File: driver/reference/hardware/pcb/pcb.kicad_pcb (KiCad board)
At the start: 2 copper layers, 122 x 122 mm, 50 parts, among them J1 USB_B_Micro, J2 USB_A, J3 USB_A, J4 USB_A, M1 Fan, Q1 S8050, SW1 SW_Push, U1 locked, U2 AT89C52, U3 SL2.1A, U4 LCD1602, Y1 11.0592MHz, Y2 12MHz

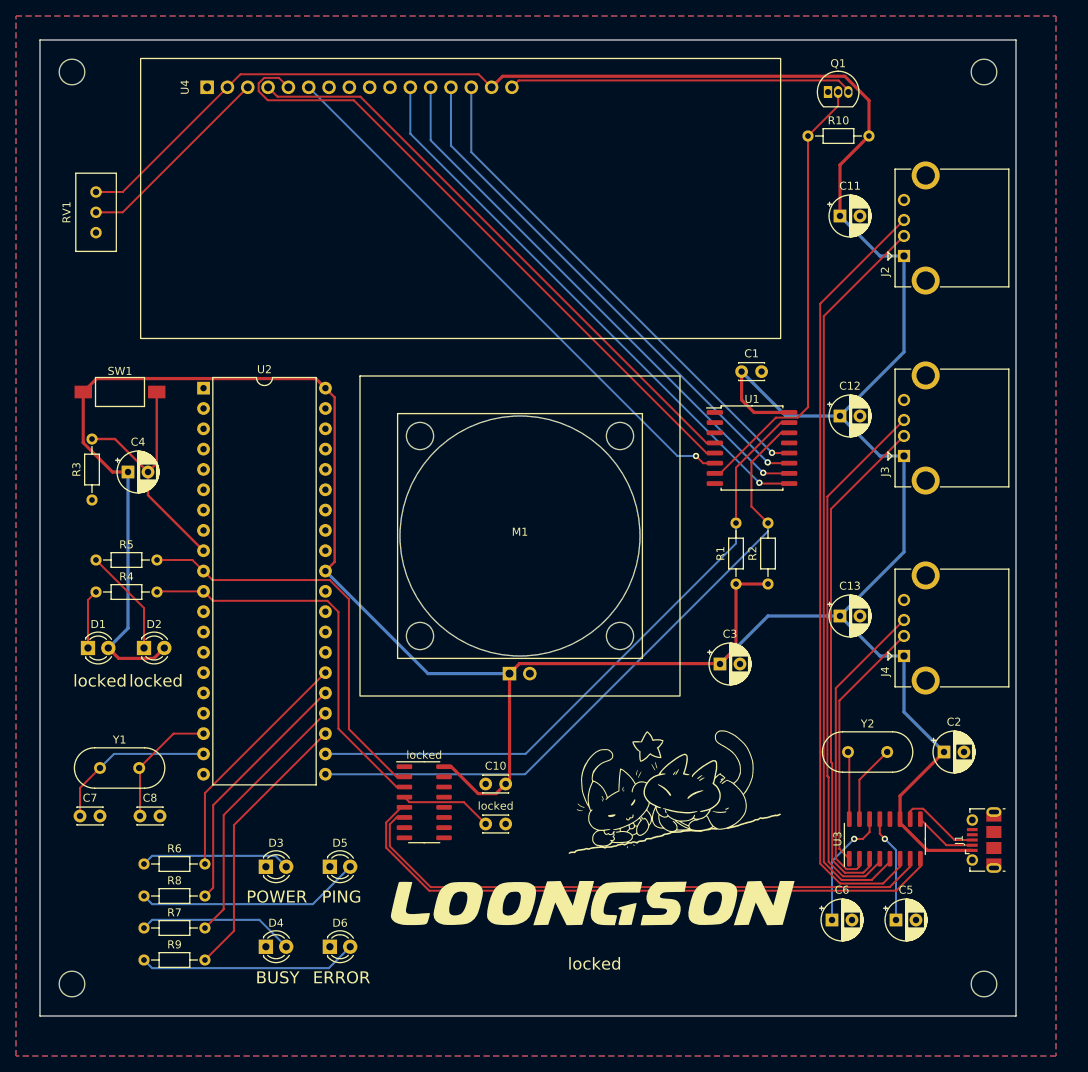
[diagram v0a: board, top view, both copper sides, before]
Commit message: Basic implementation of frontend
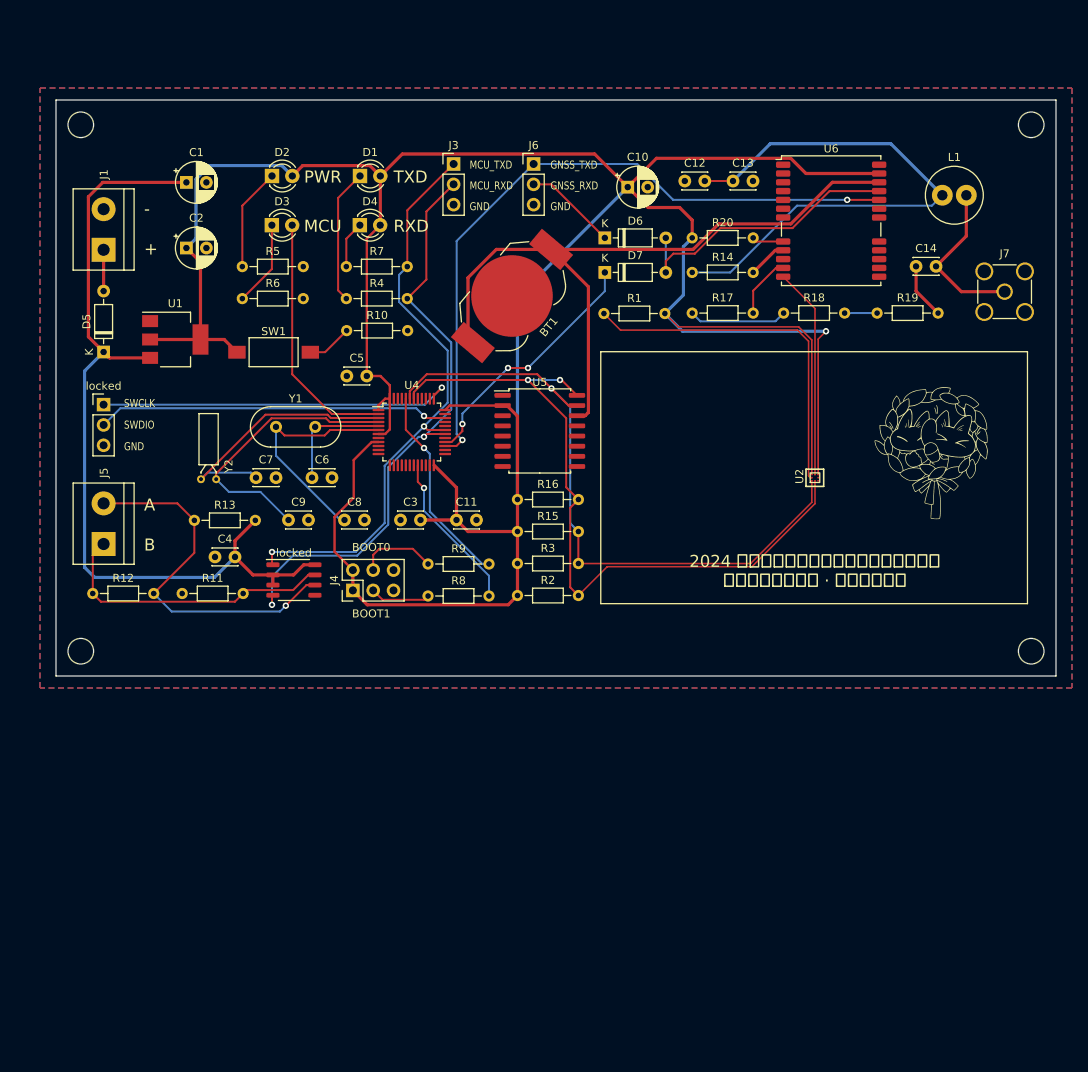
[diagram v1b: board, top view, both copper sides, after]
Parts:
- removed the G*** at (132.1, 145.8)
- removed J2: USB_A, Connector_USB:USB_A_CONNFLY_DS1095-WNR0
- removed M1: Fan, OpenStation:Fan_30x30mm
- removed Q1: S8050, Package_TO_SOT_THT:TO-92_Inline
- removed RV1: 100k, Potentiometer_THT:Potentiometer_Bourns_3296W_Vertical
- removed U3: SL2.1A, Package_SO:SOIC-16_3.9x9.9mm_P1.27mm
- removed the locked at (118.7, 136.0)
- removed the locked at (111.0, 133.3)
- added BT1: 3V, Battery:BatteryHolder_LINX_BAT-HLD-012-SMT, F.Cu at (122.0, 70.0)
- added C14: 100pF, Capacitor_THT:C_Disc_D3.0mm_W2.0mm_P2.50mm, F.Cu at (172.5, 66.3)
- added C9: 20pF, Capacitor_THT:C_Disc_D3.0mm_W2.0mm_P2.50mm, F.Cu at (94.1, 98.0)
- added D7: 1N4148, Diode_THT:D_DO-35_SOD27_P7.62mm_Horizontal, F.Cu at (133.6, 67.1)
- added J5: 485, TerminalBlock:TerminalBlock_bornier-2_P5.08mm, F.Cu at (71.0, 101.0)
- added J6: Conn_01x03, Connector_PinHeader_2.54mm:PinHeader_1x03_P2.54mm_Vertical, F.Cu at (124.7, 53.5)
- added J7: SMA, Connector_Coaxial:SMA_Amphenol_901-144_Vertical, F.Cu at (183.6, 69.5)
- added L1: 20uH, Inductor_THT:L_Radial_D7.0mm_P3.00mm, F.Cu at (175.8, 57.4)
- added R11: 10k, Resistor_THT:R_Axial_DIN0204_L3.6mm_D1.6mm_P7.62mm_Horizontal, F.Cu at (80.8, 107.2)
- added R12: 120, Resistor_THT:R_Axial_DIN0204_L3.6mm_D1.6mm_P7.62mm_Horizontal, F.Cu at (69.6, 107.2)
- added R13: 10k, Resistor_THT:R_Axial_DIN0204_L3.6mm_D1.6mm_P7.62mm_Horizontal, F.Cu at (82.3, 98.0)
- added R14: 0, Resistor_THT:R_Axial_DIN0204_L3.6mm_D1.6mm_P7.62mm_Horizontal, F.Cu at (144.5, 67.1)
- added R15: 4.7k, Resistor_THT:R_Axial_DIN0204_L3.6mm_D1.6mm_P7.62mm_Horizontal, F.Cu at (122.7, 99.4)
- added R16: 4.7k, Resistor_THT:R_Axial_DIN0204_L3.6mm_D1.6mm_P7.62mm_Horizontal, F.Cu at (122.7, 95.4)
- added R17: 0, Resistor_THT:R_Axial_DIN0204_L3.6mm_D1.6mm_P7.62mm_Horizontal, F.Cu at (144.5, 72.1)
- added R18: 0, Resistor_THT:R_Axial_DIN0204_L3.6mm_D1.6mm_P7.62mm_Horizontal, F.Cu at (156.0, 72.1)
- added R19: 0, Resistor_THT:R_Axial_DIN0204_L3.6mm_D1.6mm_P7.62mm_Horizontal, F.Cu at (167.6, 72.1)
- added R20: 10k, Resistor_THT:R_Axial_DIN0204_L3.6mm_D1.6mm_P7.62mm_Horizontal, F.Cu at (144.5, 62.7)
- added U5: DS3231M, Package_SO:SOIC-16W_7.5x10.3mm_P1.27mm, F.Cu at (125.5, 86.9)
- added U6: NEO-M8M, RF_GPS:ublox_NEO, F.Cu at (161.9, 60.6)
- added locked: Conn_01x03, Connector_PinHeader_2.54mm:PinHeader_1x03_P2.54mm_Vertical, F.Cu at (71.0, 83.6)
- added locked: MAX13487EESA, Package_SO:SOP-8_3.9x4.9mm_P1.27mm, F.Cu at (94.7, 105.5)
- C1, C10: value 0.1uF -> 10uF; footprint Capacitor_THT:C_Disc_D3.0mm_W2.0mm_P2.50mm -> Capacitor_THT:CP_Radial_D5.0mm_P2.50mm
- C11, C13, C4, C5: value 10uF -> 0.1uF; footprint Capacitor_THT:CP_Radial_D5.0mm_P2.50mm -> Capacitor_THT:C_Disc_D3.0mm_W2.0mm_P2.50mm
- C12: value locked -> 100pF; footprint Capacitor_THT:CP_Radial_D5.0mm_P2.50mm -> Capacitor_THT:C_Disc_D3.0mm_W2.0mm_P2.50mm
- C3: value 4.7uF -> 0.1uF; footprint Capacitor_THT:CP_Radial_D5.0mm_P2.50mm -> Capacitor_THT:C_Disc_D3.0mm_W2.0mm_P2.50mm
- C6: value 10uF -> 30pF; footprint Capacitor_THT:CP_Radial_D5.0mm_P2.50mm -> Capacitor_THT:C_Disc_D3.0mm_W2.0mm_P2.50mm
- C8: value 20pF -> 30pF
- D5, D6: value LED -> 1N4148; footprint LED_THT:LED_D3.0mm -> Diode_THT:D_DO-35_SOD27_P7.62mm_Horizontal
- H1, H3, H4: footprint MountingHole:MountingHole_3.2mm_M3 -> MountingHole:MountingHole_3.2mm_M3_DIN965
- H2: value MountingHole -> locked; footprint MountingHole:MountingHole_3.2mm_M3 -> MountingHole:MountingHole_3.2mm_M3_DIN965
- J1: value USB_B_Micro -> POWER; footprint Connector_USB:USB_Micro-B_Molex-105017-0001 -> TerminalBlock:TerminalBlock_bornier-2_P5.08mm
- J3: value USB_A -> Conn_01x03; footprint Connector_USB:USB_A_CONNFLY_DS1095-WNR0 -> Connector_PinHeader_2.54mm:PinHeader_1x03_P2.54mm_Vertical
- J4: value USB_A -> Conn_02x03_Odd_Even; footprint Connector_USB:USB_A_CONNFLY_DS1095-WNR0 -> Connector_PinHeader_2.54mm:PinHeader_2x03_P2.54mm_Vertical
- R10: value 4.7k -> 10k
- R2, R3: value 10k -> 4.7k
- R8, R9: value 1k -> 10k
- U1: value locked -> AMS1117-3.3; footprint Package_SO:SOIC-16W_7.5x10.3mm_P1.27mm -> Package_TO_SOT_SMD:SOT-223-3_TabPin2
- U2: value AT89C52 -> AK09911C; footprint Package_DIP:DIP-40_W15.24mm -> OpenStation:AK09911C
- U4: value LCD1602 -> STM32F103C8Tx; footprint OpenStation:LCD1602 -> Package_QFP:LQFP-48_7x7mm_P0.5mm
- Y1: value 11.0592MHz -> 8MHz
- Y2: value 12MHz -> 32.768kHz; footprint Crystal:Crystal_HC18-U_Vertical -> Crystal:Crystal_DS26_D2.0mm_L6.0mm_Horizontal
- moved J1 132.5 mm to (71.0, 64.2)
- moved C2 113.7 mm to (81.3, 64.0)
- moved C5 96.6 mm to (101.3, 80.0)
- moved D6 95.0 mm to (133.6, 62.7)
- moved D4 91.0 mm to (103.0, 61.1)
- moved R7 86.5 mm to (101.3, 66.3)
- moved Y2 86.0 mm to (85.0, 92.9), turned to 180 degrees
- moved C6 85.3 mm to (97.0, 92.7)
- moved D3 80.2 mm to (92.0, 61.1)
- moved U2 77.2 mm to (159.9, 92.7), turned to 90 degrees
- moved C10 76.7 mm to (136.5, 56.4)
- moved U1 73.4 mm to (79.9, 75.4)
- moved C1 73.3 mm to (81.3, 55.8)
- moved R6 71.7 mm to (88.3, 70.3)
- moved D5 70.3 mm to (71.0, 77.0), turned to 90 degrees
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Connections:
- C10 pad 1: GND -> +3.3V
- C10 pad 2: +5V -> GND
- C11 pad 1: +5V -> +3.3V
- C12 pad 1: +5V -> GND
- C12 pad 2: GND -> Net-(C12-Pad2)
- C13 pad 1: +5V -> Net-(C12-Pad2)
- C2 pad 1: +5V -> +3.3V
- C3 pad 1: +5V -> GND
- C3 pad 2: GND -> +3.3V
- C4 pad 1: +5V -> GND
- C4 pad 2: Net-(U2-~{RESET}) -> +5V
- C5 pad 1: Net-(U3-VDD33) -> GND
- C5 pad 2: GND -> +3.3V
- C6 pad 1: Net-(U3-VDD18) -> /MCU_XTAL0
- C7 pad 1: Net-(U2-X2) -> /MCU_OSC0
- C8 pad 1: Net-(U2-X1) -> /MCU_XTAL1
- D1 pad 2: +5V -> +3.3V
- D2 pad 2: +5V -> +3.3V
- D3 pad 1: GND -> Net-(D3-K)
- D3 pad 2: Net-(D3-A) -> /MCU_LED
- D4 pad 1: GND -> Net-(D4-K)
- D4 pad 2: Net-(D4-A) -> +3.3V
- D5 pad 1: GND -> +5V
- D6 pad 1: GND -> Net-(D6-K)
- D6 pad 2: Net-(D6-A) -> /GNSS_RXD
- J1 pad 1: +5V -> Net-(D5-A)
- J1 pad 2: /USB_DM -> GND
- J3 pad 1: +5V -> /MCU_RXD
- J3 pad 2: /USB3_DM -> /MCU_TXD
- J3 pad 3: /USB3_DP -> GND
- J4 pad 1: +5V -> +3.3V
- J4 pad 2: /USB4_DM -> +3.3V
- J4 pad 3: /USB4_DP -> Net-(J4-Pin_3)
- J4 pad 4: GND -> Net-(J4-Pin_4)
- R1 pad 1: +5V -> Net-(U2-RSTN)
- R1 pad 2: /MCU_SDA -> +3.3V
- R10 pad 1: /EXP_P3 -> Net-(R10-Pad1)
- R10 pad 2: +5V -> GND
- R2 pad 1: +5V -> +3.3V
- R3 pad 1: GND -> +3.3V
- R3 pad 2: Net-(U2-~{RESET}) -> /MCU_SDA
- R5 pad 2: /MCU_RXD -> GND
- R6 pad 1: Net-(D3-A) -> Net-(D3-K)
- R6 pad 2: /MCU_POWER -> GND
- R7 pad 1: Net-(D4-A) -> Net-(D4-K)
- R7 pad 2: /MCU_BUSY -> /MCU_RXD
- R8 pad 1: Net-(D5-A) -> Net-(J4-Pin_3)
- R8 pad 2: /MCU_PING -> /MCU_BOOT1
- R9 pad 1: Net-(D6-A) -> Net-(J4-Pin_4)
- R9 pad 2: /MCU_ERROR -> /MCU_BOOT0
- SW1 pad 1: +5V -> +3.3V
- SW1 pad 2: Net-(U2-~{RESET}) -> Net-(R10-Pad1)
- U1 pad 1: unconnected-(U1-A0-Pad1) -> GND
- U1 pad 2: unconnected-(U1-A1-Pad2) -> +3.3V
- U1 pad 3: unconnected-(U1-A2-Pad3) -> +5V
- U4 pad 1: GND -> +3.3V
- U4 pad 11: /EXP_P4 -> unconnected-(U4-PA1-Pad11)
- U4 pad 12: /EXP_P5 -> unconnected-(U4-PA2-Pad12)
- U4 pad 13: /EXP_P6 -> unconnected-(U4-PA3-Pad13)
- U4 pad 14: /EXP_P7 -> unconnected-(U4-PA4-Pad14)
- U4 pad 15: +5V -> unconnected-(U4-PA5-Pad15)
- U4 pad 16: Net-(Q1-C) -> unconnected-(U4-PA6-Pad16)
- U4 pad 2: +5V -> /MCU_LED
- U4 pad 3: Net-(U4-VO) -> /MCU_OSC0
- U4 pad 4: /EXP_P0 -> /MCU_OSC1
- U4 pad 5: /EXP_P1 -> /MCU_XTAL0
- U4 pad 6: /EXP_P2 -> /MCU_XTAL1
- U4 pad 7: unconnected-(U4-D0-Pad7) -> +3.3V
- U4 pad 8: unconnected-(U4-D1-Pad8) -> GND
- U4 pad 9: unconnected-(U4-D2-Pad9) -> +3.3V
- Y1 pad 1: Net-(U2-X2) -> /MCU_XTAL1
- Y1 pad 2: Net-(U2-X1) -> /MCU_XTAL0
- Y2 pad 1: Net-(U3-XIN) -> /MCU_OSC1
- Y2 pad 2: Net-(U3-XOUT) -> /MCU_OSC0
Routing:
- net +3.3V: track 0.00 -> 404.2 mm, vias 0 -> 1
- net +5V: track 468.8 -> 105.9 mm
- net /USB2_DP: track 97.7 -> 0.00 mm
- net /USB2_DM: track 92.5 -> 0.00 mm
- net /VBAT: track 0.00 -> 87.7 mm
- net /GNSS_TXD: track 0.00 -> 86.3 mm, vias 0 -> 2
- net /EXP_P1: track 81.2 -> 0.00 mm
- net /USB1_DP: track 77.1 -> 0.00 mm
- net /EXP_P0: track 74.3 -> 0.00 mm
- net /USB1_DM: track 74.1 -> 0.00 mm
- net /EXP_P4: track 71.3 -> 0.00 mm, vias 1 -> 0
- net /EXP_P2: track 70.2 -> 0.00 mm, vias 1 -> 0
- net Net-(C12-Pad2): track 0.00 -> 69.6 mm
- net /EXP_P5: track 68.7 -> 0.00 mm, vias 1 -> 0
- net /USB3_DP: track 67.2 -> 0.00 mm
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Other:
- board size 122 x 122 mm -> 125 x 72 mm
- board text added: "+"
- board text added: "-"
- board text added: "2024 全国大学生嵌入式芯片与系统设计竞赛 便携式卫星地面站 · 姿态参考模组"
- board text added: "A"
- board text added: "B"
- board text added: "BOOT0"
- board text added: "BOOT1"
- board text added: "GND"
- board text added: "GNSS_RXD"
- board text added: "GNSS_TXD"
- board text added: "MCU"
- board text added: "MCU_RXD"
- board text added: "MCU_TXD"
- board text added: "PWR"
- board text added: "RXD"
- board text added: "SWCLK"
- board text added: "SWDIO"
- board text added: "TXD"
- board text removed: "BUSY"
- board text removed: "ERROR"
- board text removed: "PING"
- board text removed: "POWER"
- board text removed: "locked"

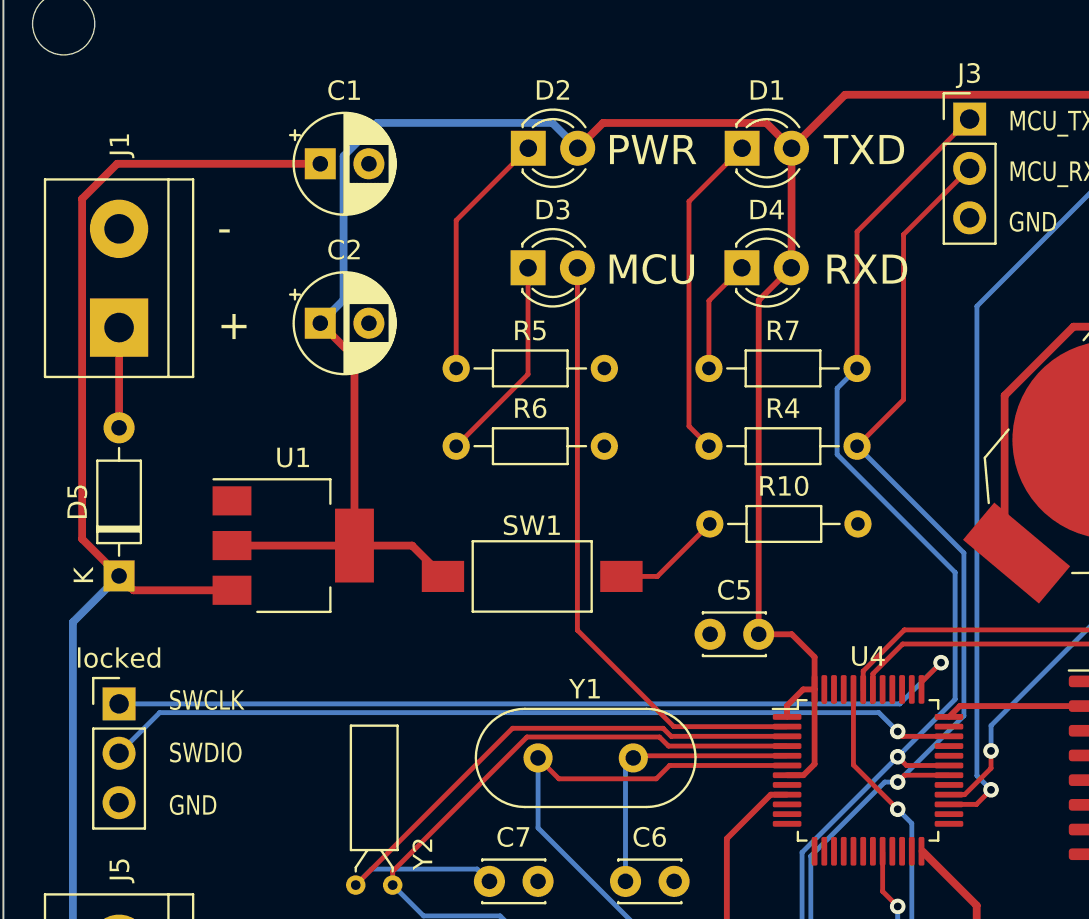
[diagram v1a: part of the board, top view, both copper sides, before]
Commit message: Updated reference board schematic & firmware
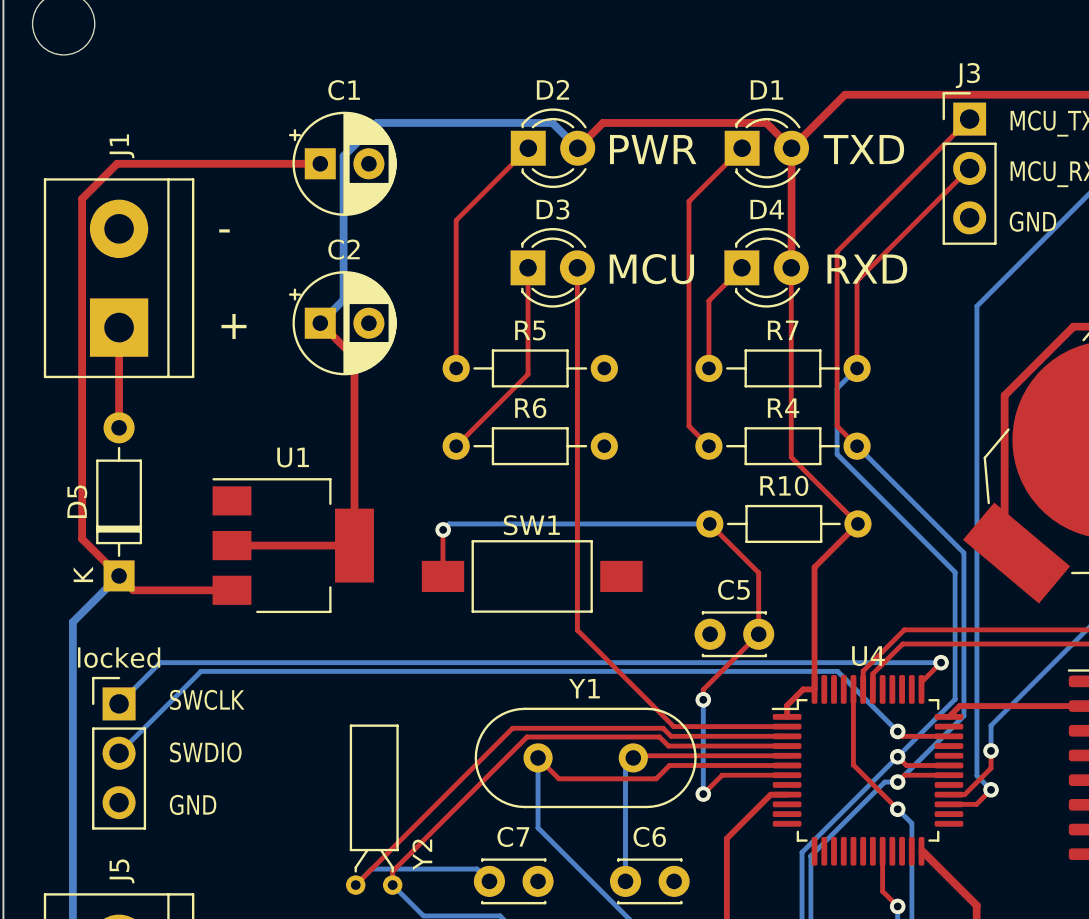
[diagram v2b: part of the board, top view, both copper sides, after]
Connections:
- C5 pad 2: +3.3V -> Net-(U4-NRST)
- J3 pad 1: /MCU_RXD -> /MCU_TXD
- J3 pad 2: /MCU_TXD -> /MCU_RXD
- R10 pad 1: Net-(R10-Pad1) -> Net-(U4-NRST)
- R10 pad 2: GND -> +3.3V
- SW1 pad 1: +3.3V -> Net-(U4-NRST)
- SW1 pad 2: Net-(R10-Pad1) -> GND
- U4 pad 7: +3.3V -> Net-(U4-NRST)
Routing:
- net Net-(U4-NRST): track 0.00 -> 37.1 mm, vias 0 -> 3
- net +3.3V: track 404.2 -> 392.9 mm
- net Net-(R10-Pad1): track 5.66 -> 0.00 mm
- net /MCU_TXD: track 75.5 -> 78.9 mm
- net /MCU_RXD: track 73.4 -> 70.8 mm
- net /MCU_SWDIO: track 44.1 -> 45.8 mm
